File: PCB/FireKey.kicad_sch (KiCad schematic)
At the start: 76 parts, among them SW1 SW_MEC_5E, U1 Arduino_Pro_Micro_USB-C

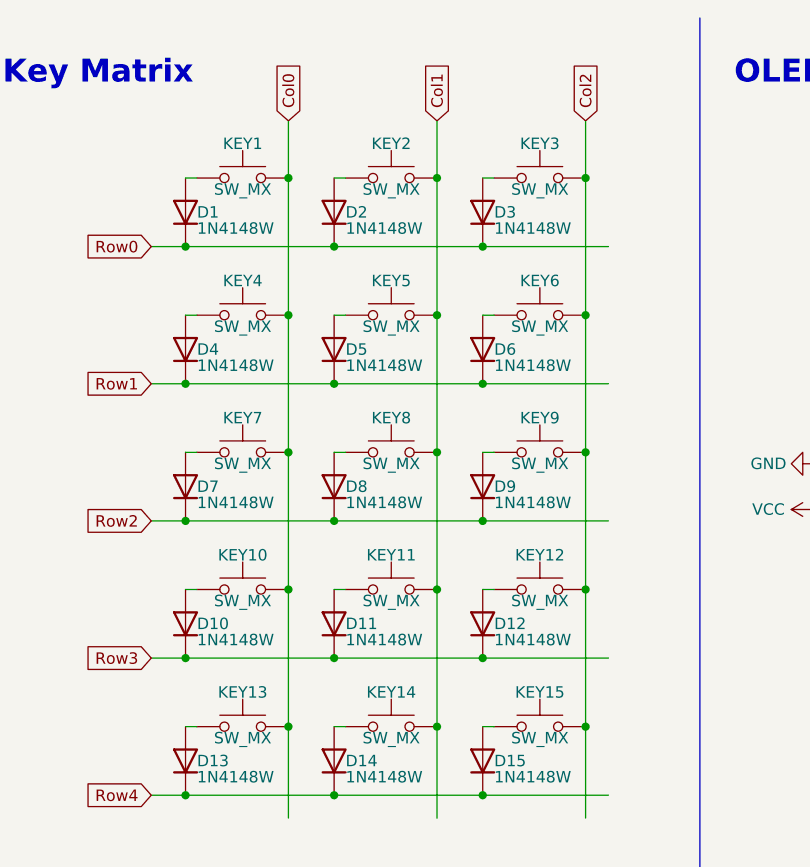
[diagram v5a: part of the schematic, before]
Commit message: make key matrix schematic represent actual layout
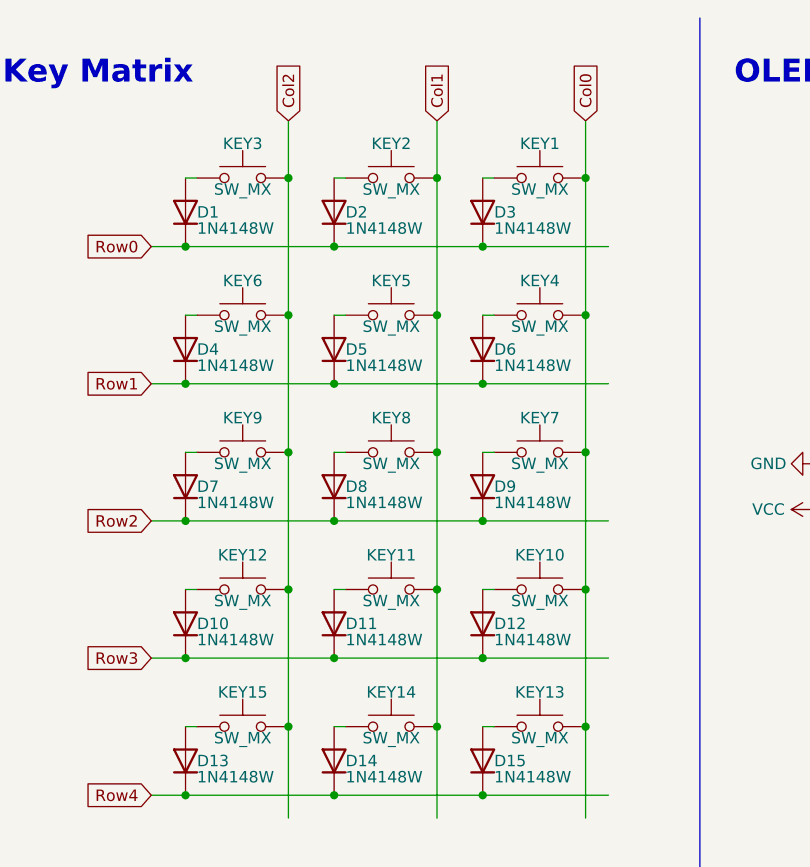
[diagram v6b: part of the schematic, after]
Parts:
- renumbered KEY3 to KEY1, KEY12 to KEY10, KEY10 to KEY12, KEY15 to KEY13, KEY13 to KEY15, KEY1 to KEY3, KEY6 to KEY4, KEY4 to KEY6, KEY9 to KEY7, KEY7 to KEY9
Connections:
- net Col0: now also KEY1.3 (B), KEY1.4 (B), KEY10.3 (B), KEY10.4 (B), KEY13.3 (B), KEY13.4 (B), KEY4.3 (B), KEY4.4 (B), KEY7.3 (B), KEY7.4 (B); no longer KEY12.3 (B), KEY12.4 (B), KEY15.3 (B), KEY15.4 (B), KEY3.3 (B), KEY3.4 (B), KEY6.3 (B), KEY6.4 (B), KEY9.3 (B), KEY9.4 (B)
- net Col2: now also KEY12.3 (B), KEY12.4 (B), KEY15.3 (B), KEY15.4 (B), KEY3.3 (B), KEY3.4 (B), KEY6.3 (B), KEY6.4 (B), KEY9.3 (B), KEY9.4 (B); no longer KEY1.3 (B), KEY1.4 (B), KEY10.3 (B), KEY10.4 (B), KEY13.3 (B), KEY13.4 (B), KEY4.3 (B), KEY4.4 (B), KEY7.3 (B), KEY7.4 (B)
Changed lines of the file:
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@@
     )
   )
-  (global_label "Col0" (shape input) (at 48.26 24.13 90) (fields_autoplaced)
+  (global_label "Col2" (shape input) (at 48.26 24.13 90) (fields_autoplaced)
     (effects (font (size 1.27 1.27)) (justify left))
     (property "Intersheet References" "${INTERSHEET_REFS}" (id 0) (at 48.1806 17.4231 90)
@@
     )
   )
-  (global_label "Col2" (shape input) (at 81.28 24.13 90) (fields_autoplaced)
+  (global_label "Col0" (shape input) (at 81.28 24.13 90) (fields_autoplaced)
     (effects (font (size 1.27 1.27)) (justify left))
     (property "Intersheet References" "${INTERSHEET_REFS}" (id 0) (at 81.2006 17.4231 90)
@@
   (symbol (lib_id "Switch:SW_MEC_5G") (at 76.2 60.96 0) (unit 1)
     (in_bom yes) (on_board yes)
-    (property "Reference" "KEY9" (id 0) (at 76.2 57.15 0))
+    (property "Reference" "KEY7" (id 0) (at 76.2 57.15 0))
     (property "Value" "SW_MX" (id 1) (at 76.2 62.23 0))
     (property "Footprint" "Button_Switch_Keyboard:SW_Cherry_MX_1.00u_PCB" (id 2) (at 76.2 55.88 0)
@@
   (symbol (lib_id "Switch:SW_MEC_5G") (at 43.18 91.44 0) (unit 1)
     (in_bom yes) (on_board yes)
-    (property "Reference" "KEY13" (id 0) (at 43.18 87.63 0))
+    (property "Reference" "KEY15" (id 0) (at 43.18 87.63 0))
     (property "Value" "SW_MX" (id 1) (at 43.18 92.71 0))
     (property "Footprint" "Button_Switch_Keyboard:SW_Cherry_MX_1.00u_PCB" (id 2) (at 43.18 86.36 0)
@@
   (symbol (lib_id "Switch:SW_MEC_5G") (at 43.18 30.48 0) (unit 1)
     (in_bom yes) (on_board yes)
-    (property "Reference" "KEY1" (id 0) (at 43.18 26.67 0))
+    (property "Reference" "KEY3" (id 0) (at 43.18 26.67 0))
     (property "Value" "SW_MX" (id 1) (at 43.18 31.75 0))
     (property "Footprint" "Button_Switch_Keyboard:SW_Cherry_MX_1.00u_PCB" (id 2) (at 43.18 25.4 0)
@@
   (symbol (lib_id "Switch:SW_MEC_5G") (at 43.18 60.96 0) (unit 1)
     (in_bom yes) (on_board yes)
-    (property "Reference" "KEY7" (id 0) (at 43.18 57.15 0))
+    (property "Reference" "KEY9" (id 0) (at 43.18 57.15 0))
     (property "Value" "SW_MX" (id 1) (at 43.18 62.23 0))
     (property "Footprint" "Button_Switch_Keyboard:SW_Cherry_MX_1.00u_PCB" (id 2) (at 43.18 55.88 0)
@@
   (symbol (lib_id "Switch:SW_MEC_5G") (at 76.2 76.2 0) (unit 1)
     (in_bom yes) (on_board yes)
-    (property "Reference" "KEY12" (id 0) (at 76.2 72.39 0))
+    (property "Reference" "KEY10" (id 0) (at 76.2 72.39 0))
     (property "Value" "SW_MX" (id 1) (at 76.2 77.47 0))
     (property "Footprint" "Button_Switch_Keyboard:SW_Cherry_MX_1.00u_PCB" (id 2) (at 76.2 71.12 0)
@@
   (symbol (lib_id "Switch:SW_MEC_5G") (at 43.18 76.2 0) (unit 1)
     (in_bom yes) (on_board yes)
-    (property "Reference" "KEY10" (id 0) (at 43.18 72.39 0))
+    (property "Reference" "KEY12" (id 0) (at 43.18 72.39 0))
     (property "Value" "SW_MX" (id 1) (at 43.18 77.47 0))
     (property "Footprint" "Button_Switch_Keyboard:SW_Cherry_MX_1.00u_PCB" (id 2) (at 43.18 71.12 0)
@@
   (symbol (lib_id "Switch:SW_MEC_5G") (at 43.18 45.72 0) (unit 1)
     (in_bom yes) (on_board yes)
-    (property "Reference" "KEY4" (id 0) (at 43.18 41.91 0))
+    (property "Reference" "KEY6" (id 0) (at 43.18 41.91 0))
     (property "Value" "SW_MX" (id 1) (at 43.18 46.99 0))
     (property "Footprint" "Button_Switch_Keyboard:SW_Cherry_MX_1.00u_PCB" (id 2) (at 43.18 40.64 0)
@@
   (symbol (lib_id "Switch:SW_MEC_5G") (at 76.2 45.72 0) (unit 1)
     (in_bom yes) (on_board yes)
-    (property "Reference" "KEY6" (id 0) (at 76.2 41.91 0))
+    (property "Reference" "KEY4" (id 0) (at 76.2 41.91 0))
     (property "Value" "SW_MX" (id 1) (at 76.2 46.99 0))
     (property "Footprint" "Button_Switch_Keyboard:SW_Cherry_MX_1.00u_PCB" (id 2) (at 76.2 40.64 0)
@@
   (symbol (lib_id "Switch:SW_MEC_5G") (at 76.2 91.44 0) (unit 1)
     (in_bom yes) (on_board yes)
-    (property "Reference" "KEY15" (id 0) (at 76.2 87.63 0))
+    (property "Reference" "KEY13" (id 0) (at 76.2 87.63 0))
     (property "Value" "SW_MX" (id 1) (at 76.2 92.71 0))
     (property "Footprint" "Button_Switch_Keyboard:SW_Cherry_MX_1.00u_PCB" (id 2) (at 76.2 86.36 0)
@@
   (symbol (lib_id "Switch:SW_MEC_5G") (at 76.2 30.48 0) (unit 1)
     (in_bom yes) (on_board yes)
-    (property "Reference" "KEY3" (id 0) (at 76.2 26.67 0))
+    (property "Reference" "KEY1" (id 0) (at 76.2 26.67 0))
     (property "Value" "SW_MX" (id 1) (at 76.2 31.75 0))
     (property "Footprint" "Button_Switch_Keyboard:SW_Cherry_MX_1.00u_PCB" (id 2) (at 76.2 25.4 0)
@@
       (reference "H12") (unit 1) (value "M3_MountingHole") (footprint "MountingHole:MountingHole_3.2mm_M3")
     )
-    (path "/545b5243-f2de-45a9-a93f-da66a30d14e3"
+    (path "/d548904c-51aa-41db-b20a-89c28d8fe025"
       (reference "KEY1") (unit 1) (value "SW_MX") (footprint "Button_Switch_Keyboard:SW_Cherry_MX_1.00u_PCB")
     )
@@
       (reference "KEY2") (unit 1) (value "SW_MX") (footprint "Button_Switch_Keyboard:SW_Cherry_MX_1.00u_PCB")
     )
-    (path "/d548904c-51aa-41db-b20a-89c28d8fe025"
+    (path "/545b5243-f2de-45a9-a93f-da66a30d14e3"
       (reference "KEY3") (unit 1) (value "SW_MX") (footprint "Button_Switch_Keyboard:SW_Cherry_MX_1.00u_PCB")
     )
-    (path "/81ed3533-8b56-4f37-8ae4-fb5da50bd426"
+    (path "/9bd7cf42-0aea-4d72-963a-0869faa5e959"
       (reference "KEY4") (unit 1) (value "SW_MX") (footprint "Button_Switch_Keyboard:SW_Cherry_MX_1.00u_PCB")
     )
@@
       (reference "KEY5") (unit 1) (value "SW_MX") (footprint "Button_Switch_Keyboard:SW_Cherry_MX_1.00u_PCB")
     )
-    (path "/9bd7cf42-0aea-4d72-963a-0869faa5e959"
+    (path "/81ed3533-8b56-4f37-8ae4-fb5da50bd426"
       (reference "KEY6") (unit 1) (value "SW_MX") (footprint "Button_Switch_Keyboard:SW_Cherry_MX_1.00u_PCB")
     )
-    (path "/61a7724b-a2af-4682-9dfa-e74357f754c4"
+    (path "/20414db2-be41-4287-8faf-850134a9b55b"
       (reference "KEY7") (unit 1) (value "SW_MX") (footprint "Button_Switch_Keyboard:SW_Cherry_MX_1.00u_PCB")
     )
@@
       (reference "KEY8") (unit 1) (value "SW_MX") (footprint "Button_Switch_Keyboard:SW_Cherry_MX_1.00u_PCB")
     )
-    (path "/20414db2-be41-4287-8faf-850134a9b55b"
+    (path "/61a7724b-a2af-4682-9dfa-e74357f754c4"
       (reference "KEY9") (unit 1) (value "SW_MX") (footprint "Button_Switch_Keyboard:SW_Cherry_MX_1.00u_PCB")
     )
-    (path "/6f2715a1-7442-4511-b2d5-9ce145803717"
+    (path "/68afd9f3-1e56-4c61-ada8-c01cdf3d9c94"
       (reference "KEY10") (unit 1) (value "SW_MX") (footprint "Button_Switch_Keyboard:SW_Cherry_MX_1.00u_PCB")
     )
@@
       (reference "KEY11") (unit 1) (value "SW_MX") (footprint "Button_Switch_Keyboard:SW_Cherry_MX_1.00u_PCB")
     )
-    (path "/68afd9f3-1e56-4c61-ada8-c01cdf3d9c94"
+    (path "/6f2715a1-7442-4511-b2d5-9ce145803717"
       (reference "KEY12") (unit 1) (value "SW_MX") (footprint "Button_Switch_Keyboard:SW_Cherry_MX_1.00u_PCB")
     )
-    (path "/3f3b9a17-95ab-4a65-9f77-c3efd0f3e9d9"
+    (path "/ad4a7ef9-8e21-49db-97bc-36bc92d2d732"
       (reference "KEY13") (unit 1) (value "SW_MX") (footprint "Button_Switch_Keyboard:SW_Cherry_MX_1.00u_PCB")
     )
@@
       (reference "KEY14") (unit 1) (value "SW_MX") (footprint "Button_Switch_Keyboard:SW_Cherry_MX_1.00u_PCB")
     )
-    (path "/ad4a7ef9-8e21-49db-97bc-36bc92d2d732"
+    (path "/3f3b9a17-95ab-4a65-9f77-c3efd0f3e9d9"
       (reference "KEY15") (unit 1) (value "SW_MX") (footprint "Button_Switch_Keyboard:SW_Cherry_MX_1.00u_PCB")
     )

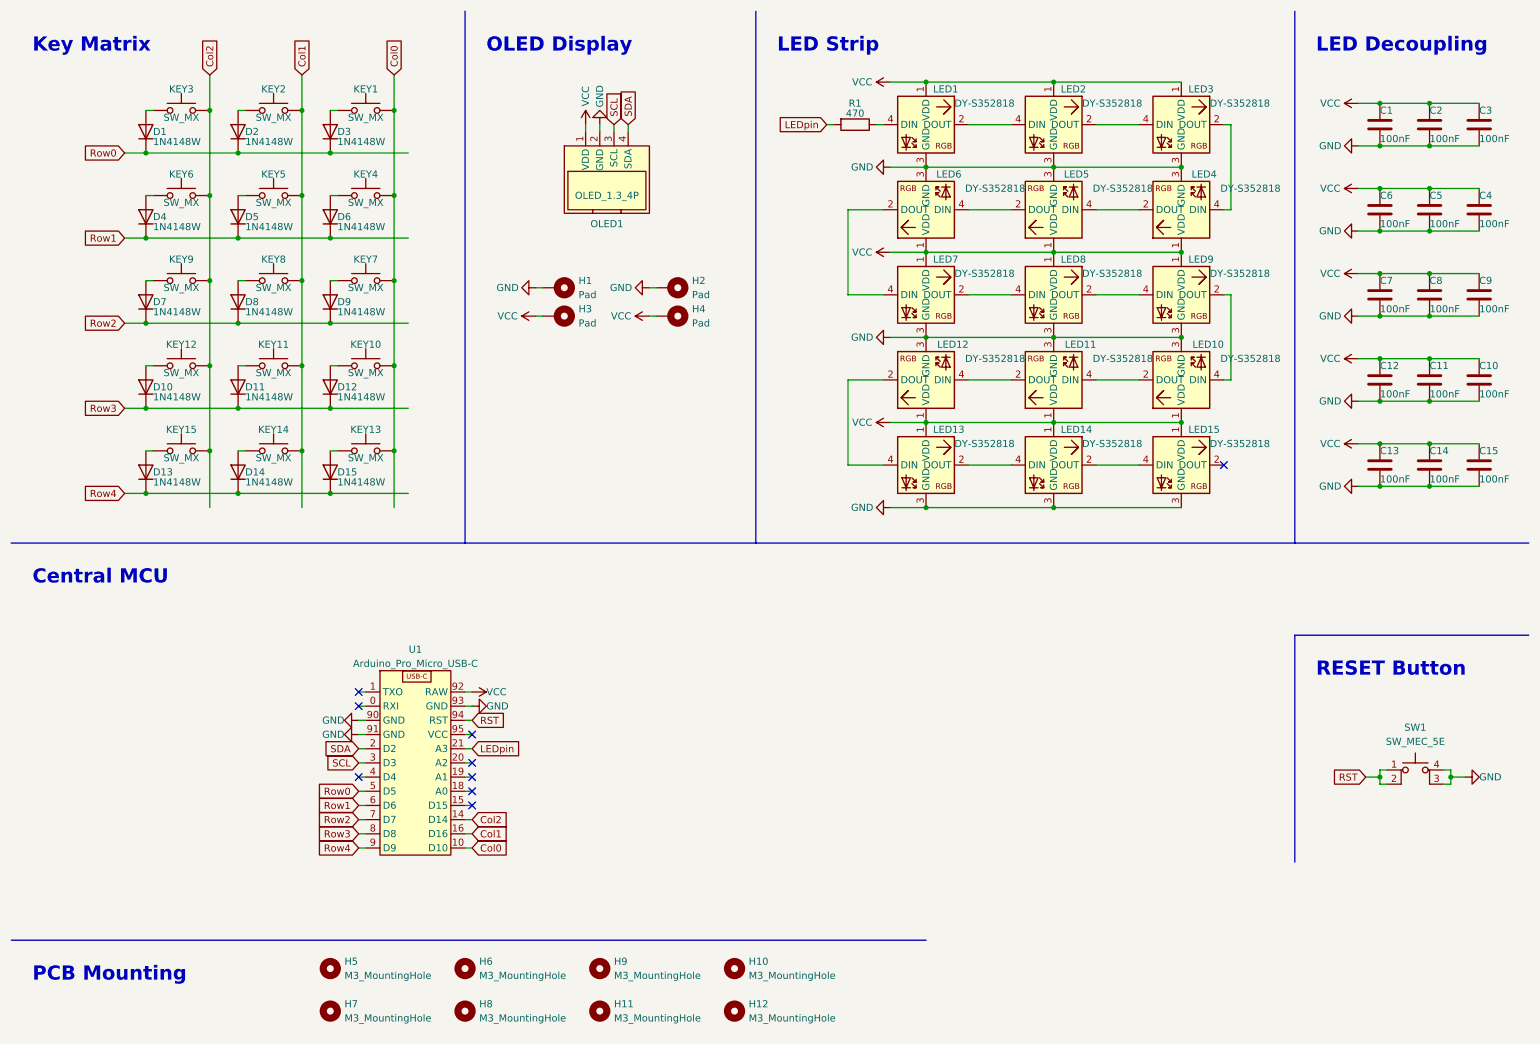
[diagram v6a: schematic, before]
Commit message: mirrored leds to match pcb; changed key numbering to match led index
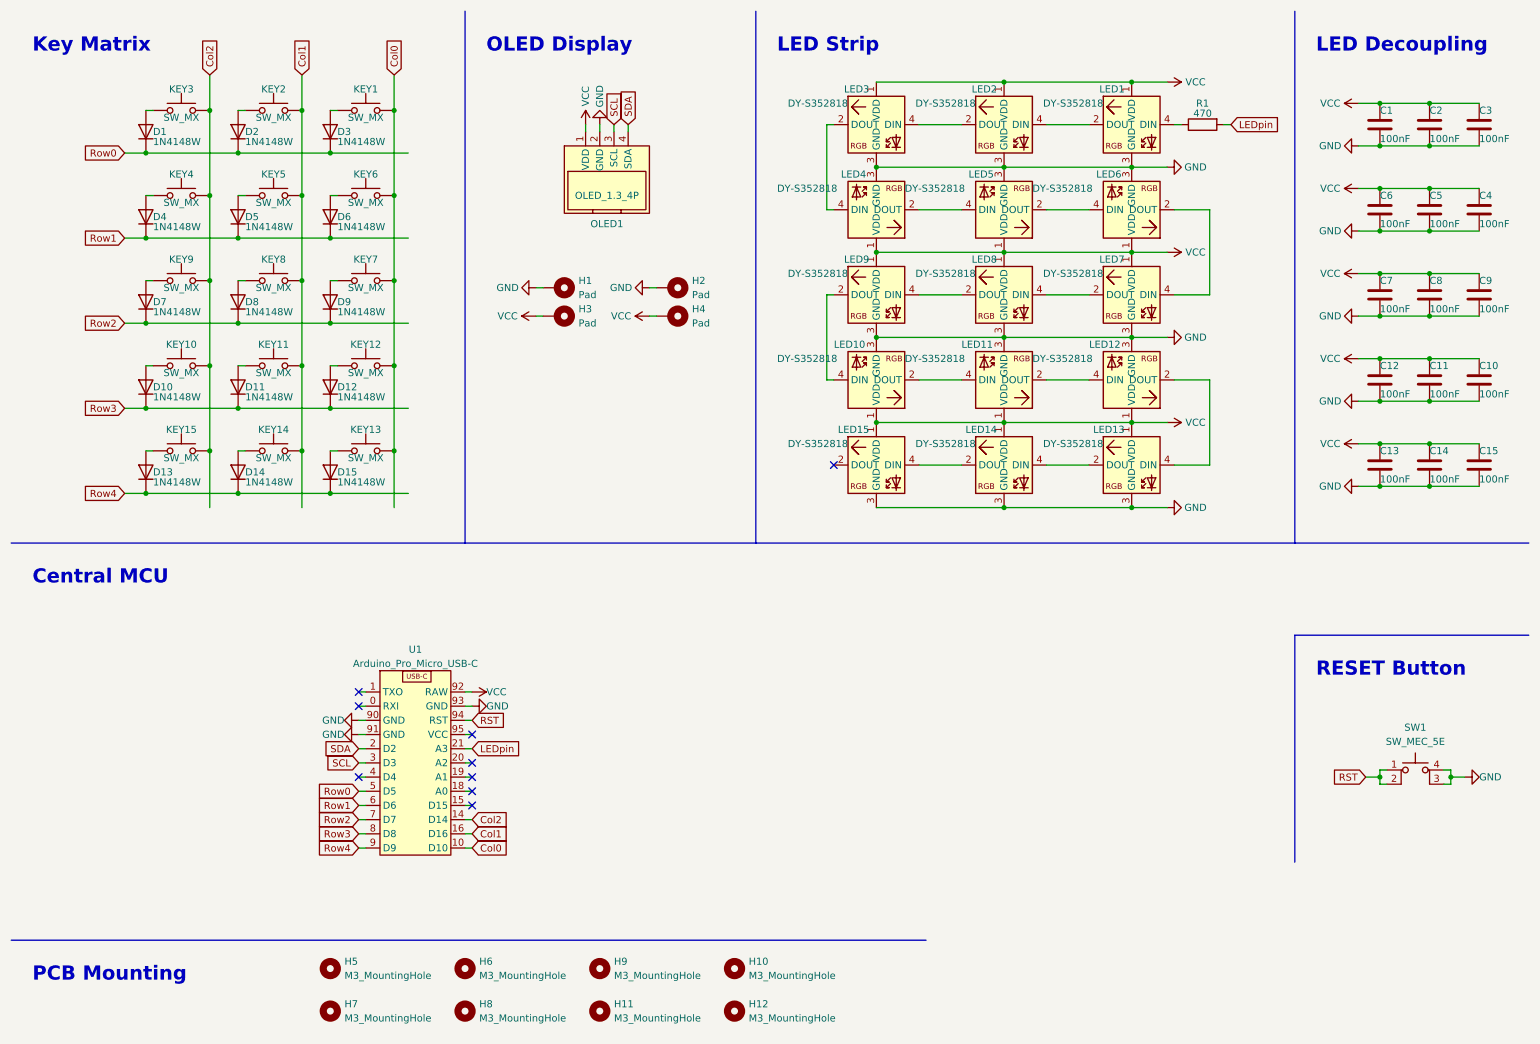
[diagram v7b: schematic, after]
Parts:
- renumbered KEY12 to KEY10, KEY10 to KEY12, KEY6 to KEY4, KEY4 to KEY6
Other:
- moved on the sheet: LED1, LED10, LED11, LED12, LED13, LED14, LED15, LED2, LED3, LED4, LED5, LED6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

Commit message: small changes to schematic
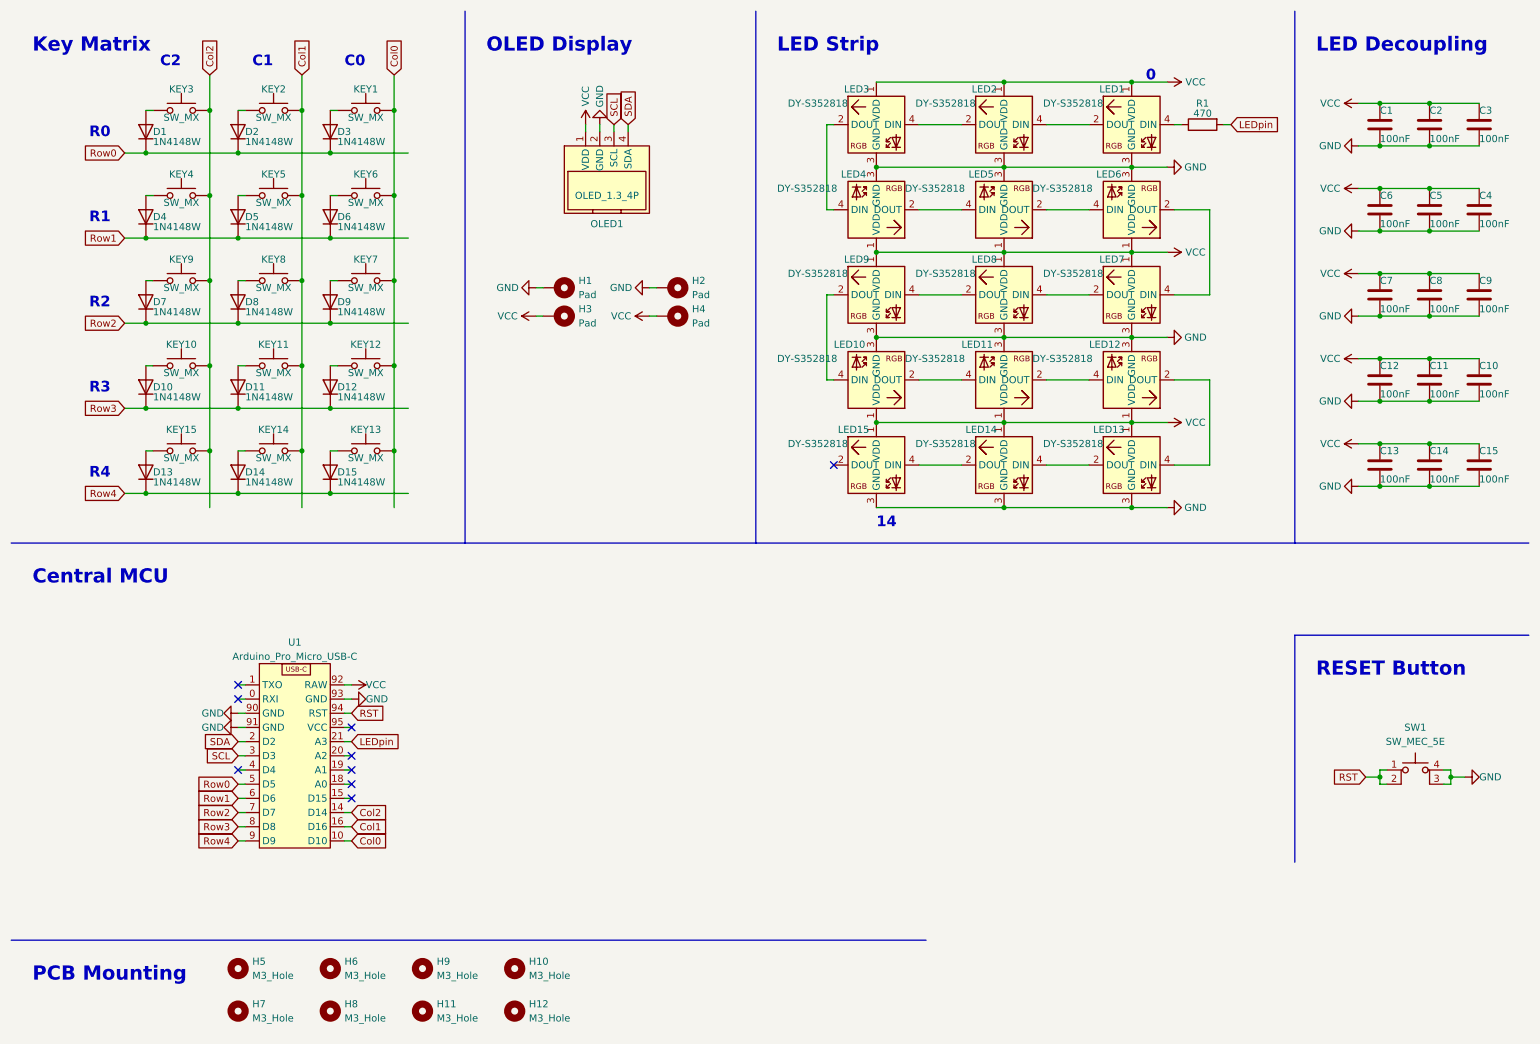
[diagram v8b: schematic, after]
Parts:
- H10, H11, H12, H5, H6, H7, H8, H9: value M3_MountingHole -> M3_Hole
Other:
- note added: "0"
- note added: "14"
- note added: "C0"
- note added: "C1"
- note added: "C2"
- note added: "R0"
- note added: "R1"
- note added: "R2"
- note added: "R3"
- note added: "R4"
- moved on the sheet: H10, H11, H12, H5, H6, H7, H8, H9, U1
